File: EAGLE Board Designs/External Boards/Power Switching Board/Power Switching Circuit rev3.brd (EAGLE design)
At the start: 93.6 x 68.1 mm, 82 parts, among them J1 CONNECTOR-3_, J2 CONNECTOR-4_SOURIAU_, J3 CONNECTOR-4_SOURIAU_, Q1 TRANSISTOR_N_MOS_2-7K1S_TK100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, Q2 TRANSISTOR_N_MOS_2-7K1S_TK100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, Q3 TRANSISTOR_N_MOS_2-7K1S_TK100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, Q4 TRANSISTOR_N_MOS_2-7K1S_TK100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, U1 LTC4421

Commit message: Replaced OV/UV resistors
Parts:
- added F2: FUSE_MB_10, HyTechDevices:MINI-BLADE_FUSE_HOLDER
- R10: value RESISTOR_0603_31.6K -> RESISTOR_0603_11.8
- R11: value RESISTOR_0603_14.3K -> RESISTOR_0603_43.2
- R3: value 14.3k -> RESISTOR_0603_5.6
- R5: value 10k -> RESISTOR_0603_11.8
- R6: value 953k -> RESISTOR_0603_1.13K
- R7: value 31.6k -> RESISTOR_0603_43.2
- R8: value RESISTOR_0603_953K -> RESISTOR_0603_1.13K
- R9: value RESISTOR_0603_10K -> RESISTOR_0603_5.6
- moved R5 860.0 mm to (-25.4, -845.8), turned to 0 degrees
- moved R6 850.9 mm to (-25.4, -838.2), turned to 0 degrees
- moved R3 603.2 mm to (-25.4, -842.0)
- moved R7 598.1 mm to (-25.4, -849.6)
- moved R11 175.3 mm to (-25.4, -864.9)
- moved R8 171.5 mm to (-25.4, -853.4)
- moved R9 171.5 mm to (-25.4, -857.2)
- moved R10 167.6 mm to (-25.4, -861.1)
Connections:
- removed net BATTERY-: J2.3, J2.4
- net BATTERY: now also F2.L1, F2.L2
- net DCDC: now also J3.1, J3.2; no longer J3.3, J3.4
- net GND: now also R11.1, R7.2; no longer R10.1, R7.1
- net N$24: now also R3.1, R5.2; no longer R3.2, R5.1
- net N$25: now also R5.1, R7.1; no longer R3.1, R7.2
- net N$27: now also R10.2; no longer R11.2
- net N$28: now also R10.1, R11.2; no longer R10.2, R11.1
- net OUT: now also F2.R1, F2.R2, J2.3, J2.4, J3.3, J3.4; no longer J3.1, J3.2
- net UVF1: now also R3.2; no longer R5.2
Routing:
- net GND: track 701.6 -> 168.2 mm
- net OUT: track 5.01 -> 22.8 mm
- net DCDC: track 40.4 -> 22.6 mm
- net UVF1: track 11.3 -> 7.85 mm

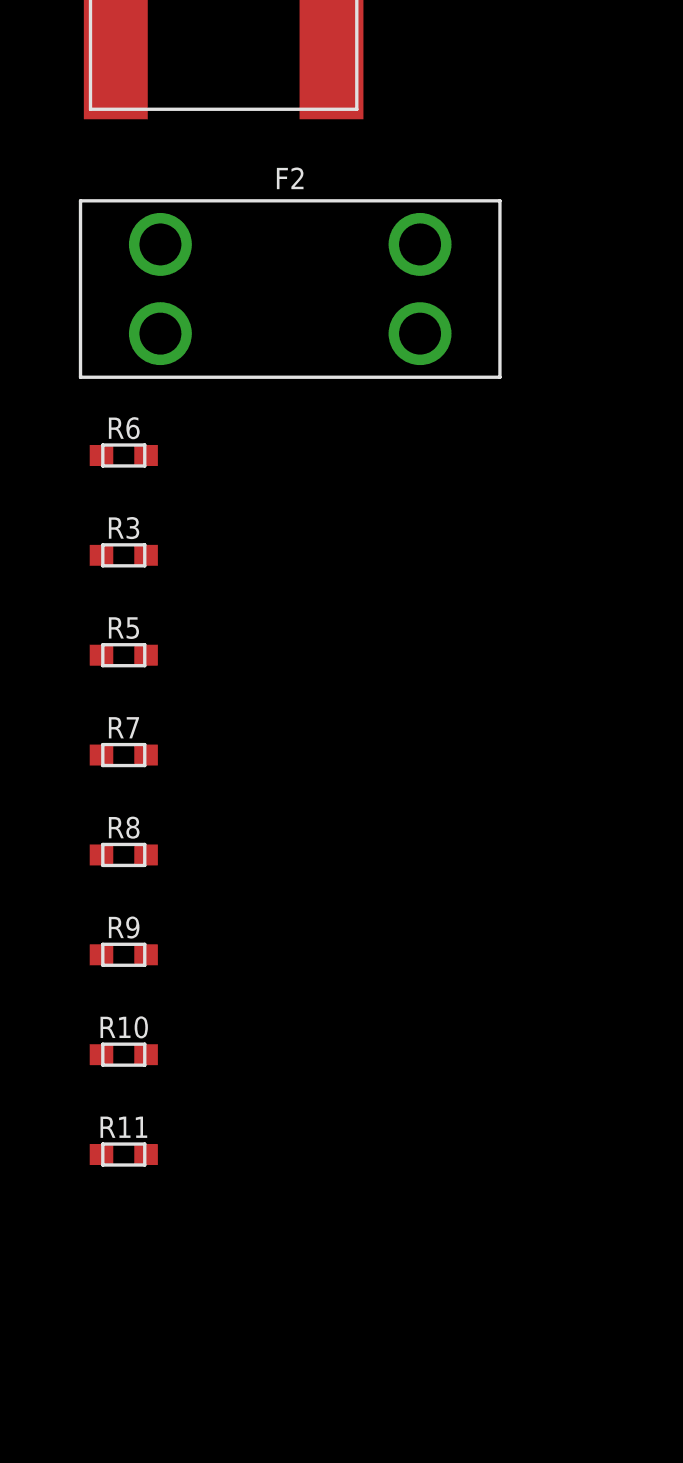
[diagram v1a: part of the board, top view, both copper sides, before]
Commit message: Added bypass fuse, other changes
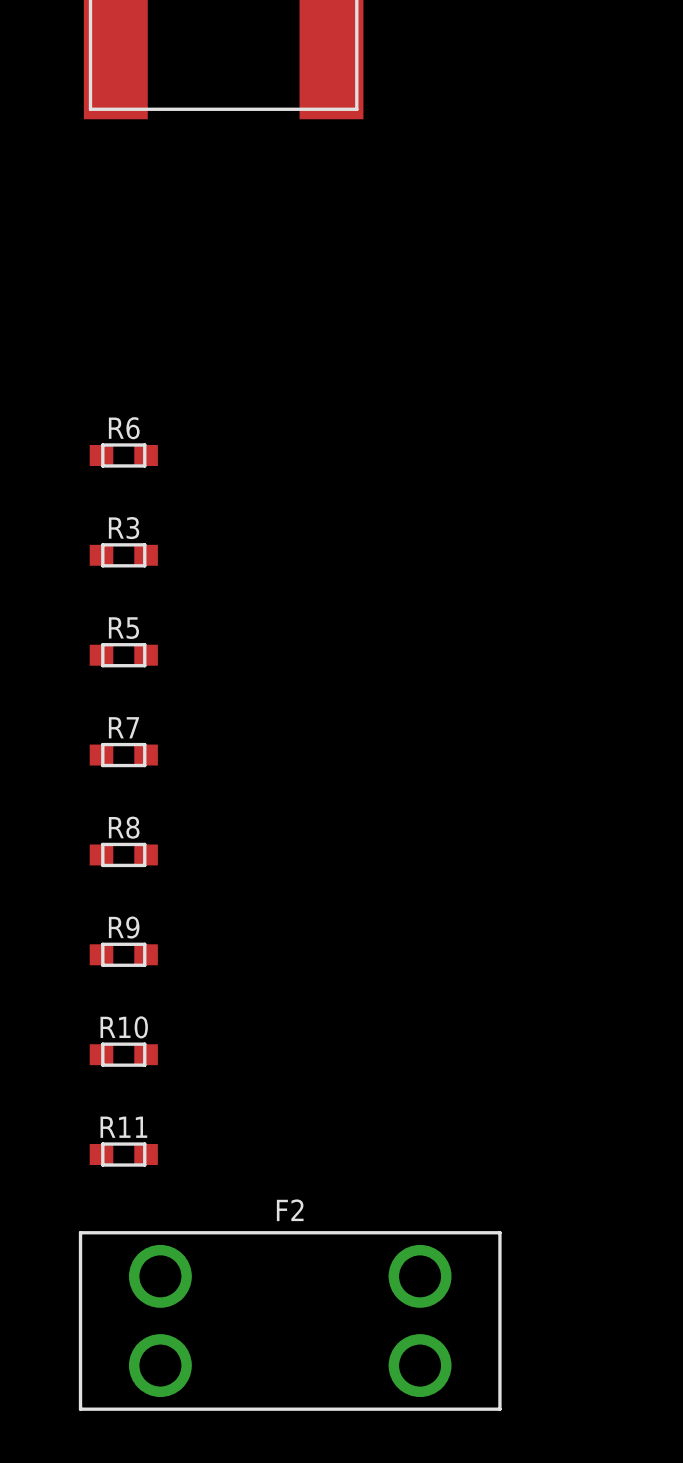
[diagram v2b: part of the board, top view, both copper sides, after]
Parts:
- moved F2 39.4 mm to (-19.1, -871.2)
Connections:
- new net DCDC_VICOR: F3.L1, F3.L2, J3.1, J3.2
- net BATTERY: now also F2.R1, F2.R2; no longer F2.L1, F2.L2
- net DCDC: no longer F3.L1, F3.L2, J3.1, J3.2
- net OUT: now also F2.L1, F2.L2; no longer F2.R1, F2.R2
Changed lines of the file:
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@@
 <attribute name="VOLTAGE" value="0.077V" x="-21.59" y="-821.69" size="1.778" layer="27" display="off"/>
-</element>
-<element name="F2" library="HyTechDevices" package="MINI-BLADE_FUSE_HOLDER" value="FUSE_MB_10" x="-19.05" y="-831.85" smashed="yes">
-<attribute name="CURRENT" value="10A" x="-19.05" y="-831.85" size="1.778" layer="27" display="off"/>
-<attribute name="DKPN" value="F991-ND" x="-19.05" y="-831.85" size="1.778" layer="27" display="off"/>
-<attribute name="MANUFACTURER" value="Littelfuse Inc." x="-19.05" y="-831.85" size="1.778" layer="27" display="off"/>
-<attribute name="MOPN" value="576-0297010.WXNV" x="-19.05" y="-831.85" size="1.778" layer="27" display="off"/>
-<attribute name="MPN" value="0297010.WXNV" x="-19.05" y="-831.85" size="1.778" layer="27" display="off"/>
-<attribute name="NAME" x="-19.05" y="-828.04" size="0.8128" layer="25" font="vector" align="bottom-center"/>
-<attribute name="VOLTAGE" value="32V" x="-19.05" y="-831.85" size="1.778" layer="27" display="off"/>
 </element>
 <element name="R6" library="HyTechDevices" package="0603-RES" value="RESISTOR_0603_1.13K" x="-25.4" y="-838.2" smashed="yes">
@@
 <attribute name="VOLTAGE_CONTINUOUS" value="75V" x="-25.4" y="-864.87" size="1.778" layer="27" display="off"/>
 <attribute name="VOLTAGE_MAX" value="150V" x="-25.4" y="-864.87" size="1.778" layer="27" display="off"/>
+</element>
+<element name="F2" library="HyTechDevices" package="MINI-BLADE_FUSE_HOLDER" value="FUSE_MB_10" x="-19.05" y="-871.22" smashed="yes">
+<attribute name="CURRENT" value="10A" x="-19.05" y="-871.22" size="1.778" layer="27" display="off"/>
+<attribute name="DKPN" value="F991-ND" x="-19.05" y="-871.22" size="1.778" layer="27" display="off"/>
+<attribute name="MANUFACTURER" value="Littelfuse Inc." x="-19.05" y="-871.22" size="1.778" layer="27" display="off"/>
+<attribute name="MOPN" value="576-0297010.WXNV" x="-19.05" y="-871.22" size="1.778" layer="27" display="off"/>
+<attribute name="MPN" value="0297010.WXNV" x="-19.05" y="-871.22" size="1.778" layer="27" display="off"/>
+<attribute name="NAME" x="-19.05" y="-867.41" size="0.8128" layer="25" font="vector" align="bottom-center"/>
+<attribute name="VOLTAGE" value="32V" x="-19.05" y="-871.22" size="1.778" layer="27" display="off"/>
 </element>
 </elements>
@@
 <contactref element="D1" pad="3"/>
 <contactref element="F3" pad="R1"/>
-<contactref element="F3" pad="L1"/>
 <contactref element="R2" pad="2"/>
-<contactref element="F3" pad="L2"/>
 <contactref element="F3" pad="R2"/>
 <contactref element="R13" pad="2"/>
-<contactref element="J3" pad="2"/>
-<contactref element="J3" pad="1"/>
 <contactref element="R6" pad="2"/>
 <wire x1="-24.55" y1="-754.38" x2="-24.55" y2="-838.2" width="0" layer="19" extent="1-1"/>
-<wire x1="-9.906" y1="-567.7408" x2="-24.55" y2="-754.38" width="0" layer="19" extent="1-1"/>
-<wire x1="-9.906" y1="-564.3372" x2="-9.906" y2="-567.7408" width="0" layer="19" extent="1-1"/>
-<wire x1="0" y1="-567.7408" x2="-9.906" y2="-567.7408" width="0" layer="19" extent="1-1"/>
+<wire x1="0" y1="-567.7408" x2="-24.55" y2="-754.38" width="0" layer="19" extent="1-1"/>
 <wire x1="0" y1="-564.3372" x2="0" y2="-567.7408" width="0" layer="19" extent="1-1"/>
-<wire x1="-24.35" y1="-515.62" x2="-9.906" y2="-564.3372" width="0" layer="19" extent="1-1"/>
+<wire x1="-24.35" y1="-515.62" x2="0" y2="-564.3372" width="0" layer="19" extent="1-1"/>
 <wire x1="-2.3" y1="-77.7206" x2="-24.35" y2="-515.62" width="0" layer="19" extent="1-1"/>
 <wire x1="-12.954" y1="6.8453" x2="-2.3" y2="-77.7206" width="0" layer="19" extent="1-1"/>
 <wire x1="-3.8608" y1="22.6568" x2="-12.954" y2="6.8453" width="0" layer="19" extent="1-1"/>
-<wire x1="-12.292403125" y1="27.882115625" x2="-3.8608" y2="22.6568" width="0" layer="19" extent="1-1"/>
-<wire x1="-16.451690625" y1="25.64945" x2="-12.292403125" y2="27.882115625" width="0" layer="19" extent="1-1"/>
 </signal>
 <signal name="RIGHT_BRB">
@@
 <contactref element="J2" pad="4"/>
 <contactref element="J2" pad="3"/>
-<contactref element="F2" pad="R1"/>
-<contactref element="F2" pad="R2"/>
+<contactref element="F2" pad="L2"/>
+<contactref element="F2" pad="L1"/>
 <wire x1="-24.65" y1="-198.12" x2="-26.15" y2="-201.93" width="0" layer="19" extent="1-1"/>
 <wire x1="-17.3228" y1="8.89" x2="-24.65" y2="-198.12" width="0" layer="19" extent="1-1"/>
@@
 <wire x1="-17.4752" y1="-811.149" x2="-24.55" y2="-640.08" width="0" layer="19" extent="1-1"/>
 <wire x1="-17.4752" y1="-822.579" x2="-17.4752" y2="-811.149" width="0" layer="19" extent="1-1"/>
-<wire x1="-14.097" y1="-830.1482" x2="-17.4752" y2="-822.579" width="0" layer="19" extent="1-1"/>
-<wire x1="-14.097" y1="-833.5518" x2="-14.097" y2="-830.1482" width="0" layer="19" extent="1-1"/>
+<wire x1="-24.003" y1="-869.5182" x2="-17.4752" y2="-822.579" width="0" layer="19" extent="1-1"/>
+<wire x1="-24.003" y1="-872.9218" x2="-24.003" y2="-869.5182" width="0" layer="19" extent="1-1"/>
 </signal>
 <signal name="!FAULT2">
@@
 <contactref element="F1" pad="L1"/>
 <contactref element="F1" pad="L2"/>
-<contactref element="F2" pad="L2"/>
-<contactref element="F2" pad="L1"/>
-<wire x1="-24.003" y1="-830.1482" x2="-24.003" y2="-833.5518" width="0" layer="19" extent="1-1"/>
-<wire x1="-9.906" y1="-535.5336" x2="-24.003" y2="-830.1482" width="0" layer="19" extent="1-1"/>
+<contactref element="F2" pad="R1"/>
+<contactref element="F2" pad="R2"/>
+<wire x1="-14.097" y1="-869.5182" x2="-14.097" y2="-872.9218" width="0" layer="19" extent="1-1"/>
+<wire x1="-9.906" y1="-535.5336" x2="-14.097" y2="-869.5182" width="0" layer="19" extent="1-1"/>
 <wire x1="-9.906" y1="-532.13" x2="-9.906" y2="-535.5336" width="0" layer="19" extent="1-1"/>
 <wire x1="43.423021875" y1="24.6961375" x2="-9.906" y2="-532.13" width="0" layer="19" extent="1-1"/>
@@
 <wire x1="11.4074" y1="26.5176" x2="-25.7048" y2="-822.579" width="0" layer="19" extent="1-1"/>
 </signal>
+<signal name="DCDC_VICOR">
+<contactref element="F3" pad="L1"/>
+<contactref element="F3" pad="L2"/>
+<contactref element="J3" pad="2"/>
+<contactref element="J3" pad="1"/>
+<wire x1="-9.906" y1="-564.3372" x2="-9.906" y2="-567.7408" width="0" layer="19" extent="1-1"/>
+<wire x1="-16.451690625" y1="25.64945" x2="-9.906" y2="-564.3372" width="0" layer="19" extent="1-1"/>
+<wire x1="-12.292403125" y1="27.882115625" x2="-16.451690625" y2="25.64945" width="0" layer="19" extent="1-1"/>
+</signal>
 </signals>

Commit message: Finishing touches
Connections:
- removed net RIGHT_BRB: J1.B
- net GLVMS: now also J1.B
- net OUT: no longer J3.3, J3.4
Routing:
- net OUT: track 22.8 -> 5.01 mm
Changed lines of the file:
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@@
 <wire x1="-3.8608" y1="22.6568" x2="-12.954" y2="6.8453" width="0" layer="19" extent="1-1"/>
-</signal>
-<signal name="RIGHT_BRB">
-<contactref element="J1" pad="B"/>
-<wire x1="4.881634375" y1="-20.1373625" x2="4.617965625" y2="-20.1373625" width="0.6096" layer="1"/>
 </signal>
 <signal name="START">
@@
 <contactref element="R1" pad="2"/>
 <contactref element="R19" pad="2"/>
-<contactref element="J3" pad="4"/>
-<contactref element="J3" pad="3"/>
-<wire x1="-12.328" y1="10.0928" x2="-12.954" y2="10.7188" width="1.016" layer="1"/>
-<wire x1="-12.954" y1="21.687740625" x2="-13.3200875" y2="22.053828125" width="1.016" layer="1"/>
-<wire x1="-12.954" y1="10.7188" x2="-12.954" y2="11.43" width="1.016" layer="1"/>
-<wire x1="-12.954" y1="11.43" x2="-12.954" y2="21.687740625" width="1.016" layer="1"/>
-<wire x1="-12.954" y1="11.43" x2="-13.5382" y2="10.8458" width="0.4064" layer="1"/>
-<wire x1="-13.5382" y1="10.8458" x2="-15.367" y2="10.8458" width="0.4064" layer="1"/>
-<wire x1="-15.367" y1="10.8458" x2="-17.3228" y2="8.89" width="0.4064" layer="1"/>
 <contactref element="J2" pad="4"/>
 <contactref element="J2" pad="3"/>
@@
 <contactref element="F2" pad="L1"/>
 <wire x1="-24.65" y1="-198.12" x2="-26.15" y2="-201.93" width="0" layer="19" extent="1-1"/>
-<wire x1="-17.3228" y1="8.89" x2="-24.65" y2="-198.12" width="0" layer="19" extent="1-1"/>
-<wire x1="-9.14756875" y1="24.361534375" x2="-13.3200875" y2="22.053828125" width="0" layer="19" extent="1-1"/>
-<wire x1="10.331659375" y1="10.532628125" x2="-12.328" y2="10.0928" width="0" layer="19" extent="1-1"/>
-<wire x1="15.56425" y1="6.219278125" x2="10.331659375" y2="10.532628125" width="0" layer="19" extent="1-1"/>
+<wire x1="15.56425" y1="6.219278125" x2="-24.65" y2="-198.12" width="0" layer="19" extent="1-1"/>
+<wire x1="10.331659375" y1="10.532628125" x2="15.56425" y2="6.219278125" width="0" layer="19" extent="1-1"/>
 <wire x1="24.5098" y1="23.824003125" x2="17.551471875" y2="8.2065" width="0" layer="19" extent="1-16"/>
 <wire x1="24.509803125" y1="23.824" x2="24.5098" y2="23.824003125" width="0" layer="19" extent="16-16"/>
@@
 <signal name="GLVMS">
 <contactref element="D4" pad="1"/>
+<contactref element="J1" pad="B"/>
+<wire x1="4.881634375" y1="-20.1373625" x2="4.617965625" y2="-20.1373625" width="0.6096" layer="1"/>
+<wire x1="11.221403125" y1="-13.79759375" x2="4.881634375" y2="-20.1373625" width="0" layer="19" extent="1-1"/>
 </signal>
 <signal name="N$16">

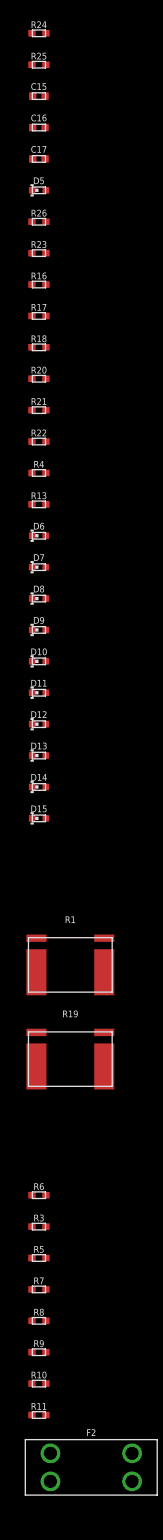
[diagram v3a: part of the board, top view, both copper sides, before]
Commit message: Fixed xml issue
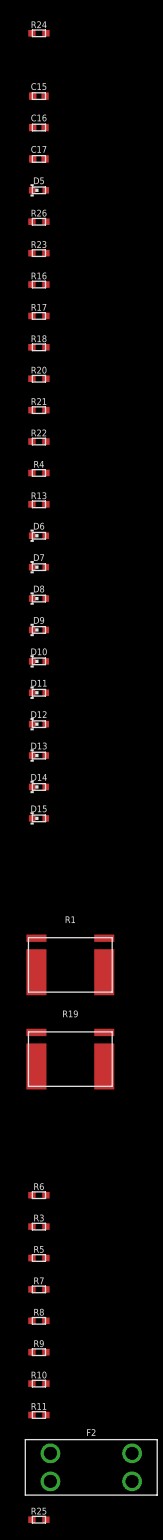
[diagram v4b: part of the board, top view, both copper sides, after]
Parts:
- moved R25 176.5 mm to (-25.4, -877.6)
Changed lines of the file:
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@@
 <attribute name="VOLTAGE_MAX" value="" x="-25.4" y="-697.23" size="1.778" layer="27" display="off"/>
-</element>
-<element name="R25" library="HyTechDevices" package="0603-RES" value="RESISTOR_0603_DNP" x="-25.4" y="-701.04" smashed="yes">
-<attribute name="DKPN" value="" x="-25.4" y="-701.04" size="1.778" layer="27" display="off"/>
-<attribute name="MANUFACTURER" value="" x="-25.4" y="-701.04" size="1.778" layer="27" display="off"/>
-<attribute name="MOPN" value="" x="-25.4" y="-701.04" size="1.778" layer="27" display="off"/>
-<attribute name="MPN" value="" x="-25.4" y="-701.04" size="1.778" layer="27" display="off"/>
-<attribute name="NAME" x="-25.4" y="-700.405" size="0.8128" layer="25" font="vector" align="bottom-center"/>
-<attribute name="POWER" value="" x="-25.4" y="-701.04" size="1.778" layer="27" display="off"/>
-<attribute name="RESISTANCE" value="DNP" x="-25.4" y="-701.04" size="1.778" layer="27" display="off"/>
-<attribute name="TOLERANCE" value="" x="-25.4" y="-701.04" size="1.778" layer="27" display="off"/>
-<attribute name="VOLTAGE_CONTINUOUS" value="" x="-25.4" y="-701.04" size="1.778" layer="27" display="off"/>
-<attribute name="VOLTAGE_MAX" value="" x="-25.4" y="-701.04" size="1.778" layer="27" display="off"/>
 </element>
 <element name="C15" library="HyTechDevices" package="0603-CAP" value="CAPACITOR_0603_25V_0.1UF" x="-25.4" y="-704.85" smashed="yes">
@@
 <attribute name="NAME" x="-19.05" y="-867.41" size="0.8128" layer="25" font="vector" align="bottom-center"/>
 <attribute name="VOLTAGE" value="32V" x="-19.05" y="-871.22" size="1.778" layer="27" display="off"/>
+</element>
+<element name="R25" library="HyTechDevices" package="0603-RES" value="RESISTOR_0603_DNP" x="-25.4" y="-877.57" smashed="yes">
+<attribute name="DKPN" value="" x="-25.4" y="-877.57" size="1.778" layer="27" display="off"/>
+<attribute name="MANUFACTURER" value="" x="-25.4" y="-877.57" size="1.778" layer="27" display="off"/>
+<attribute name="MOPN" value="" x="-25.4" y="-877.57" size="1.778" layer="27" display="off"/>
+<attribute name="MPN" value="" x="-25.4" y="-877.57" size="1.778" layer="27" display="off"/>
+<attribute name="NAME" x="-25.4" y="-876.935" size="0.8128" layer="25" font="vector" align="bottom-center"/>
+<attribute name="POWER" value="" x="-25.4" y="-877.57" size="1.778" layer="27" display="off"/>
+<attribute name="RESISTANCE" value="DNP" x="-25.4" y="-877.57" size="1.778" layer="27" display="off"/>
+<attribute name="TOLERANCE" value="" x="-25.4" y="-877.57" size="1.778" layer="27" display="off"/>
+<attribute name="VOLTAGE_CONTINUOUS" value="" x="-25.4" y="-877.57" size="1.778" layer="27" display="off"/>
+<attribute name="VOLTAGE_MAX" value="" x="-25.4" y="-877.57" size="1.778" layer="27" display="off"/>
 </element>
 </elements>
@@
 <contactref element="Q3" pad="2"/>
 <contactref element="R12" pad="2"/>
-<contactref element="R25" pad="2"/>
 <contactref element="C15" pad="1"/>
 <contactref element="R4" pad="2"/>
 <contactref element="U1" pad="30"/>
 <contactref element="R8" pad="2"/>
-<wire x1="-24.55" y1="-701.04" x2="-26.15" y2="-704.85" width="0" layer="19" extent="1-1"/>
+<contactref element="R25" pad="2"/>
 <wire x1="-24.55" y1="-750.57" x2="-26.15" y2="-704.85" width="0" layer="19" extent="1-1"/>
-<wire x1="-26.15" y1="-624.84" x2="-24.55" y2="-701.04" width="0" layer="19" extent="1-1"/>
+<wire x1="-26.15" y1="-624.84" x2="-26.15" y2="-704.85" width="0" layer="19" extent="1-1"/>
 <wire x1="-26.15" y1="-621.03" x2="-26.15" y2="-624.84" width="0" layer="19" extent="1-1"/>
 <wire x1="-24.35" y1="-519.43" x2="-26.15" y2="-621.03" width="0" layer="19" extent="1-1"/>
@@
 <wire x1="26.67" y1="-481.33" x2="26.67" y2="-485.14" width="0" layer="19" extent="1-1"/>
 <wire x1="-24.55" y1="-853.44" x2="-24.55" y2="-750.57" width="0" layer="19" extent="1-1"/>
+<wire x1="-24.55" y1="-877.57" x2="-24.55" y2="-853.44" width="0" layer="19" extent="1-1"/>
 <wire x1="-2.3" y1="-58.0206" x2="26.67" y2="-481.33" width="0" layer="19" extent="1-1"/>
 <wire x1="24.13" y1="-10.9347" x2="-2.3" y2="-58.0206" width="0" layer="19" extent="1-1"/>
@@
 <contactref element="R25" pad="1"/>
 <contactref element="R25" pad="1"/>
-<wire x1="-24.55" y1="-697.23" x2="-26.25" y2="-701.04" width="0" layer="19" extent="1-1"/>
+<wire x1="-26.25" y1="-877.57" x2="-24.55" y2="-697.23" width="0" layer="19" extent="1-1"/>
 <wire x1="26.67" y1="-488.95" x2="-24.55" y2="-697.23" width="0" layer="19" extent="1-1"/>
 </signal>

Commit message: Replaced fuses with fuse holders
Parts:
- removed F2: FUSE_MB_10, HyTechDevices:MINI-BLADE_FUSE_HOLDER
- added XF1: FUSE_HOLDER_MINIBLADESMD, HyTechDevices:3588
- F1, F3, F4: value FUSE_MB_10 -> FUSE_HOLDER_SMD; device HyTechDevices:MINI-BLADE_FUSE_HOLDER -> HyTechDevices:3588
- moved F1 397.0 mm to (-4.95, -930.8)
- moved F3 346.0 mm to (-4.95, -912.1)
- moved F4 311.2 mm to (-4.95, -893.3)
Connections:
- net BATTERY: now also F1.1, F1.2, XF1.1, XF1.2; no longer F1.L1, F1.L2, F2.R1, F2.R2
- net DCDC: now also F3.3, F3.4; no longer F3.R1, F3.R2
- net DCDC_VICOR: now also F3.1, F3.2; no longer F3.L1, F3.L2
- net N$12: now also F1.3, F1.4; no longer F1.R1, F1.R2
- net OUT: now also F4.1, F4.2, F4.3, F4.4, XF1.3, XF1.4; no longer F2.L1, F2.L2, F4.L1, F4.L2, F4.R1, F4.R2

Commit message: Fixed test points
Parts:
- removed U$11, U$7, U$8, U$9: TEST_POINT, HyTechDevices:MICRO_MINIATURE
- added TP2, TP3, TP4, TP5: TEST_POINT, HyTechDevices:MICRO_MINIATURE
- moved TP1 486.4 mm to (-22.9, -951.2)
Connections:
- net CPO: now also TP2.1; no longer U$9.1
- net GATE2: now also TP3.1; no longer U$7.1
- net GND: now also TP5.1; no longer U$11.1
- net INTVDD: now also TP4.1; no longer U$8.1
